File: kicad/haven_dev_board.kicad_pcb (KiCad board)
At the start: 6 copper layers, 72.9 x 160.9 mm, 89 parts, among them CN1 BM46B-12DS-0.35V(51).1, J1 CLE-107-01-G-DV.1, Q1 CSD23382F4.1, Q2 CSD13380F3T.1, Q3 CSD13380F3T.1, SW1 TS2819A 230GF.1, U1 BMX160.1, U10 SN74AXC4T774RSVR.1, U12 GT-USB-9047A.1, U13 SPH0641LU4H-1.1, U14 MX25R6435FBFIL0.1, U15 ADAU1860BCBZRL.1, U2 BQ25120AYFPR.1, U3 AP22916BCA4-7.1, U4 XL-0201SURC.1, U5 KTD2026.1, U6 BQ27220YZFR.1, U8 1MΩ.1, U9 AP22916BCA4-7.1, X1 Q13FC1350000200.1

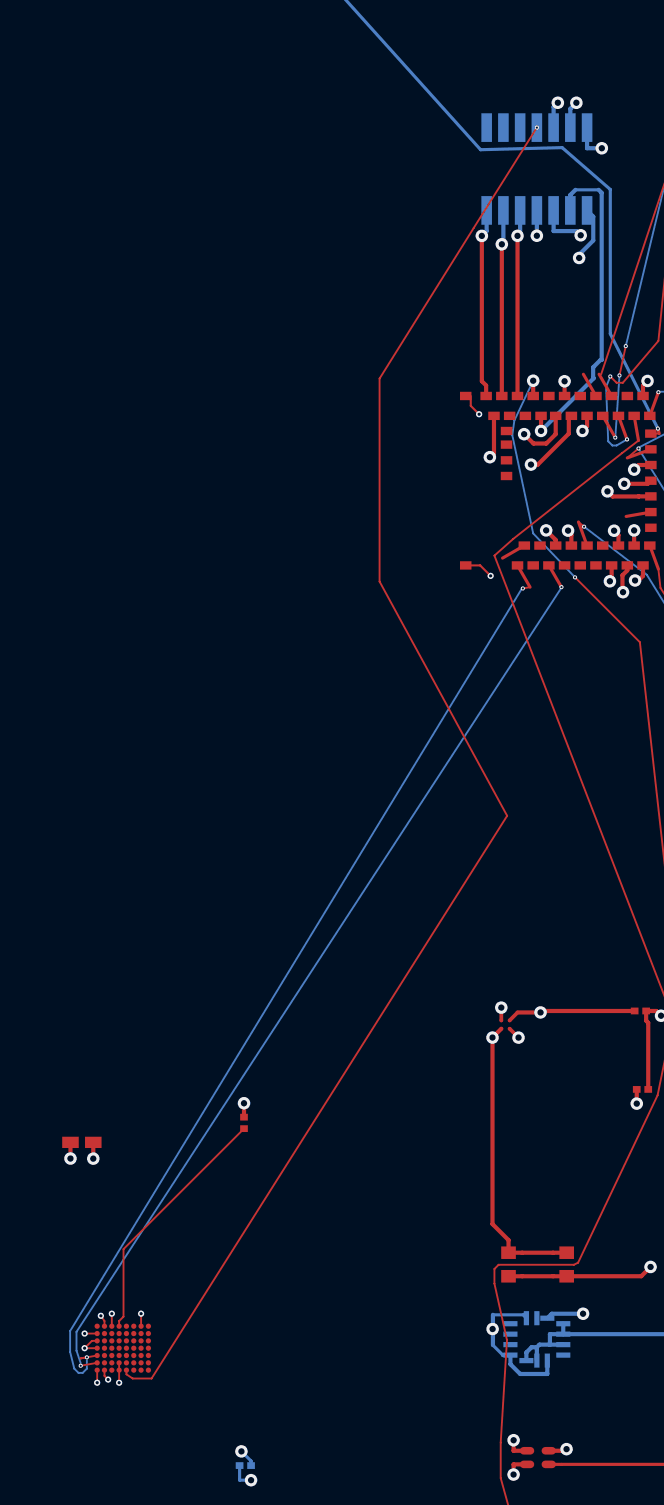
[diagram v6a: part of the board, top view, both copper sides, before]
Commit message: Build a bus-aware router; confirms TDI/TDO/TMS are genuinely blocked
Added tools/bus_router.py: routes a group of related nets together
(hardest-first ordering, each member seen as a real obstacle by
whichever routes after it) instead of one at a time, which is what
TCK/TDI/TDO/TMS actually needed -- net-by-net routing let TCK claim
the one shared escape lane and left the other three with nothing.

Two real bugs caught and fixed while building it, before trusting any
output: the endpoint-layer-fix helper computed a via position but
never added the actual connecting jog track to reach it (would have
silently disconnected the via from the true pad); and the single-layer
fast path was skipped whenever a net's start/end pads were on
different real layers, forcing the much slower general multi-layer
search even in cases (like TCK) where a fast single-layer attempt
already works fine once the wrong-layer landing is corrected
afterward -- exactly the technique used by hand earlier this session.

Extended multilayer_route.py with multilayer_astar_mixed and route_bus
with a mutual_clearance_mm option, so bus siblings can be told to run
tighter to each other than to unrelated copper (standard practice for
a real bus) without a global clearance relaxation.

Ran the actual test: hardest-first ordering alone placed TCK but left
TDI/TDO/TMS with no path at all (100k+ search states exhausted each,
not a resource limit). Adding mutual sibling clearance down to 0.05mm
between all four -- about as tight as anything used elsewhere this
session -- still left all three with nothing. This is a genuine
physical capacity limit, not an ordering or clearance-scoping problem:
the shared corridor is only wide enough for one trace's worth of
copper plus its required margins, confirmed by actual computation
rather than assumed. TDI, TDO, TMS move to the confirmed-blocked list
alongside the other BGA-interior pads -- a placement decision, not a
routing task, would be needed to free real room for 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
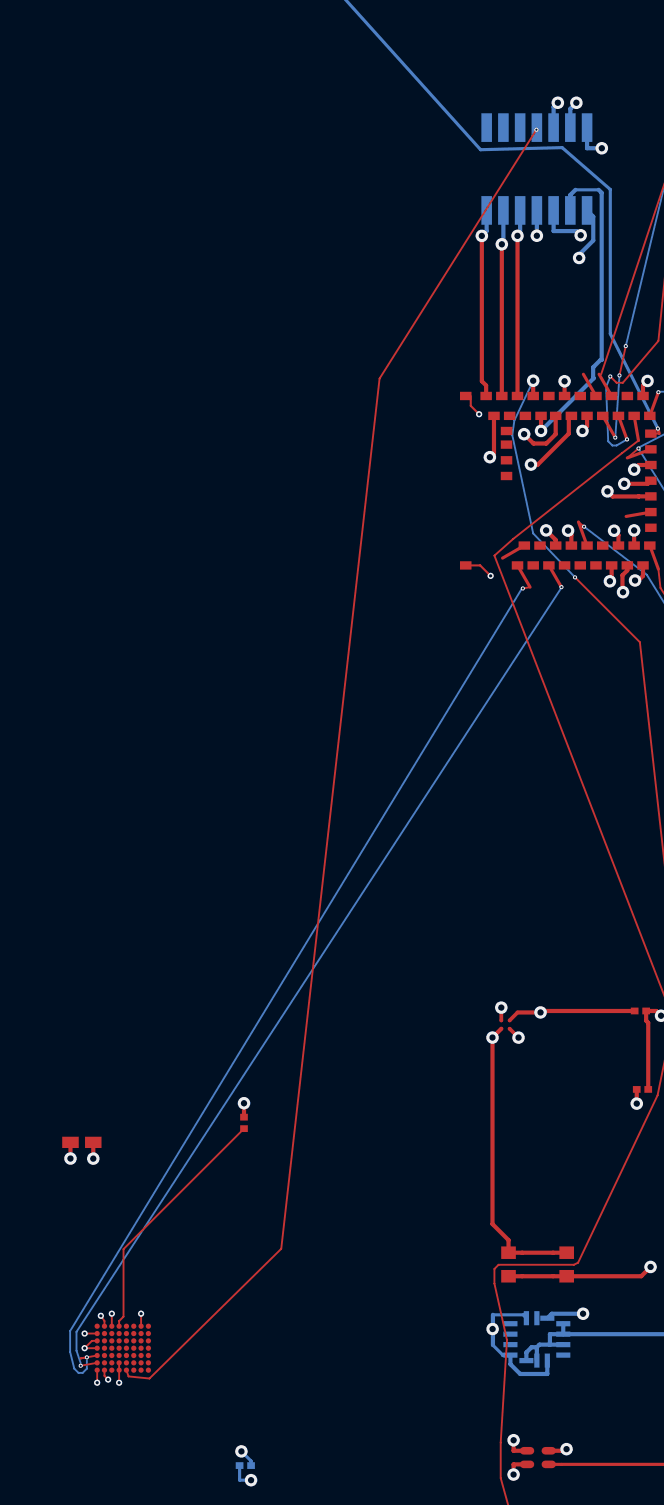
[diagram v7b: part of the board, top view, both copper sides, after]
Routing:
- net TCK: track 69.9 -> 66.2 mm
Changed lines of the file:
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@@
 	)
 	(segment
-		(start 58.7904 112.4979)
-		(end 58.7904 112.6977)
+		(start 58.8904 112.7977)
+		(end 59.8904 112.8977)
 		(width 0.09)
 		(layer "F.Cu")
@@
 	)
 	(segment
-		(start 75.3904 57.8977)
-		(end 78.4102 53.0977)
+		(start 58.7904 112.4979)
+		(end 58.7904 112.4977)
 		(width 0.09)
 		(layer "F.Cu")
@@
 	)
 	(segment
-		(start 58.7904 112.6977)
-		(end 59.090399 112.8977)
+		(start 59.8904 112.8977)
+		(end 66.1904 106.6977)
 		(width 0.09)
 		(layer "F.Cu")
@@
 	(segment
 		(start 70.8904 65.0977)
-		(end 75.3904 57.8977)
+		(end 78.3904 53.1977)
 		(width 0.09)
 		(layer "F.Cu")
@@
 	)
 	(segment
-		(start 59.090399 112.8977)
-		(end 59.9904 112.8977)
-		(width 0.09)
-		(layer "F.Cu")
-		(net 66)
-	)
-	(segment
-		(start 70.8904 74.7977)
+		(start 66.1904 106.6977)
 		(end 70.8904 65.0977)
 		(width 0.09)
@@
 	)
 	(segment
-		(start 59.9904 112.8977)
-		(end 76.9904 85.9977)
-		(width 0.09)
-		(layer "F.Cu")
-		(net 66)
-	)
-	(segment
-		(start 76.9904 85.9977)
-		(end 70.8904 74.7977)
+		(start 58.7904 112.4977)
+		(end 58.8904 112.7977)
 		(width 0.09)
 		(layer "F.Cu")
@@
 	)
 	(via
-		(at 78.4102 53.0977)
+		(at 78.3904 53.1977)
 		(size 0.2)
 		(drill 0.1)
@@
 		(net 66)
 	)
+	(segment
+		(start 78.3904 53.1977)
+		(end 78.4102 53.0977)
+		(width 0.09)
+		(layer "B.Cu")
+		(net 66)
+	)

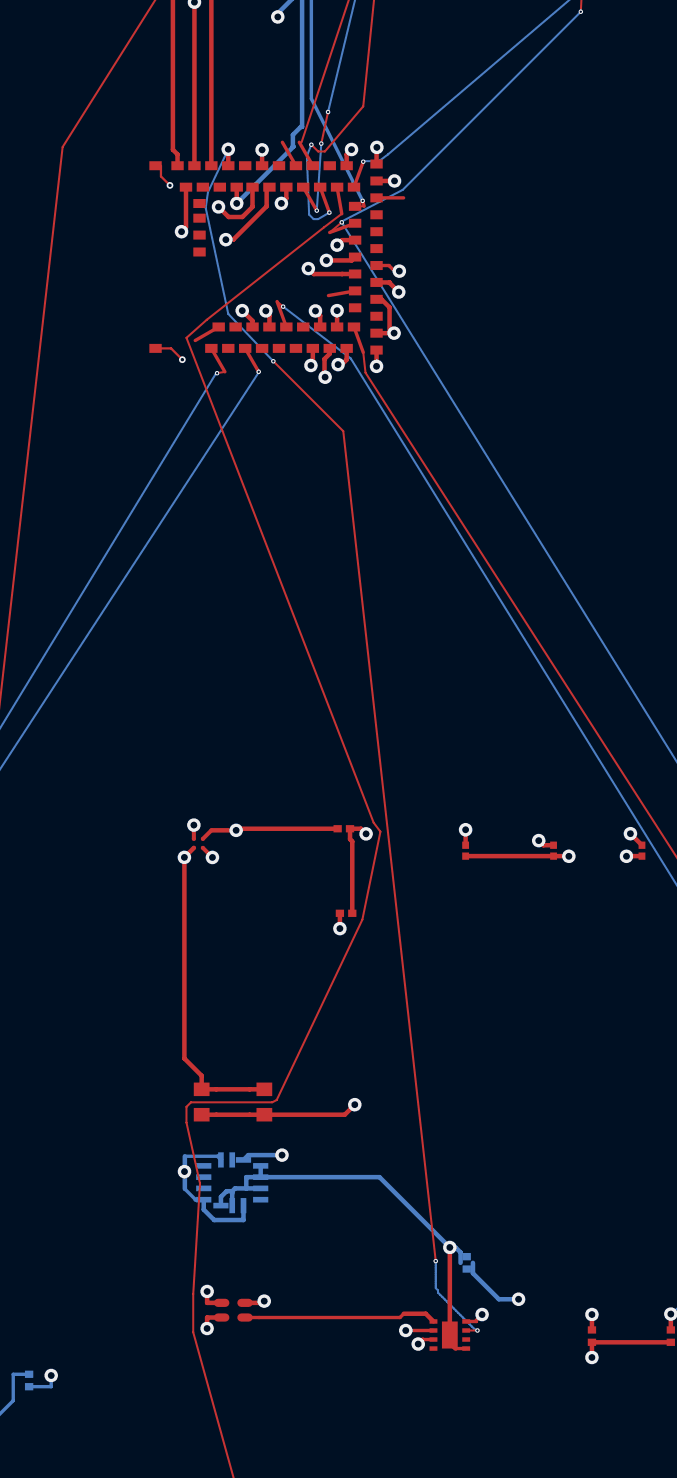
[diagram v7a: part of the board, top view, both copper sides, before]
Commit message: Route SDA (MDBT531-U5): fix a real zone-clearance workflow gap
The MDBT531-to-U5 SDA link was previously reported as walled off (a
flood-fill from the MDBT531 side supposedly reached only a tiny 6x4mm
pocket). Re-running a full-region flood-fill this session found that
claim was stale/wrong -- the whole path between MDBT531 and U5 is
reachable, and multilayer_astar finds a real route.

Placing it first surfaced a genuine, previously-unknown gap: two of the
board's four inner layers are near-full-board GND pours, and via_clear
never checked vias against filled zone copper at all -- only pads and
tracks. Adding a via near U5 triggered 8 new zone-clearance violations
(23 instances) on the first attempt.

Tried making zone fills hard obstacles in route_lib.py's obstacle
collectors, but that produces false negatives: checking a new via
against the *stale* fill (computed before the via existed) makes any
via anywhere near a ground pour look permanently blocked, even though
187 vias already coexist fine with these same pours via the fill
algorithm's automatic per-via clearance carve-out. Reverted that and
added `route_lib.refill_zones()` instead -- call it after placing new
copper and before Save()/DRC, so the saved fill polygons are accurate.
With that, the same route is 0 new violations, 40->39 unconnected.

Co-Authored-By: Claude Sonnet 5 <noreply@anthropic.com>
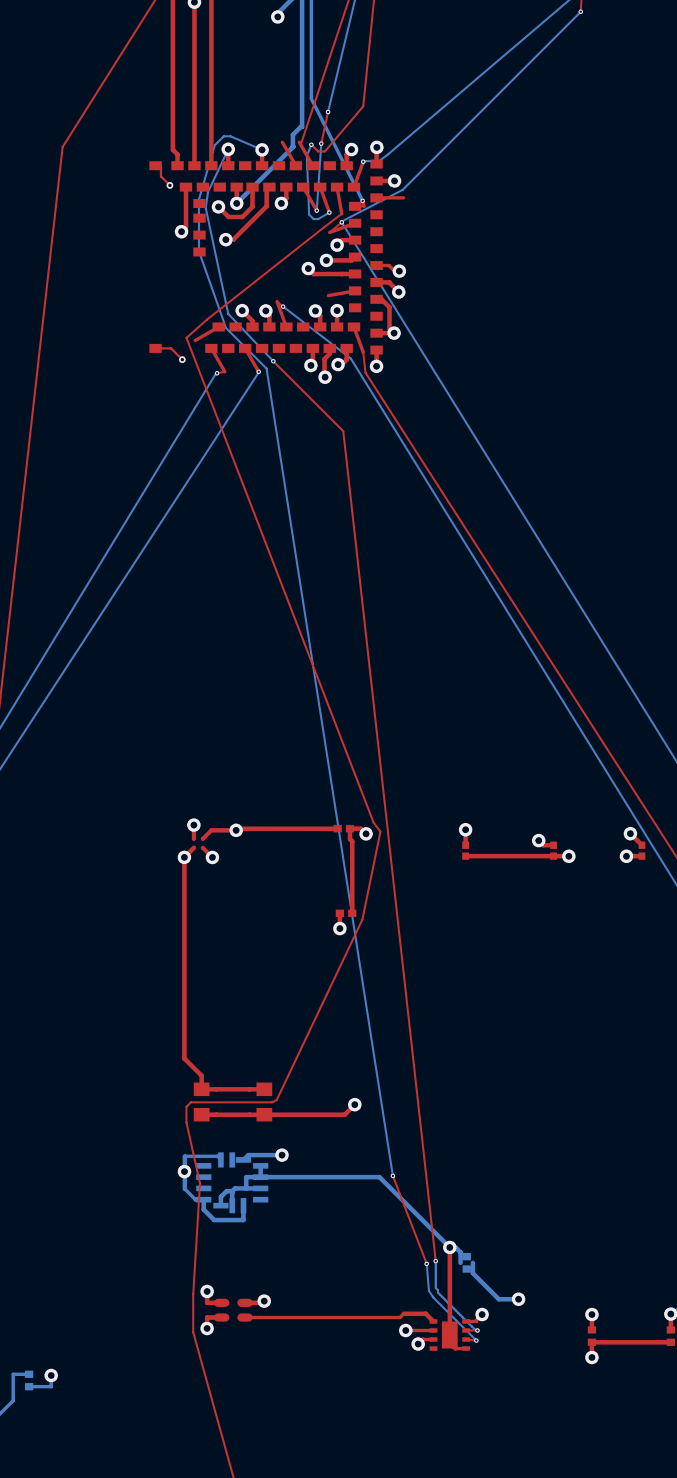
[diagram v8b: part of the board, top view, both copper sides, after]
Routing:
- net SDA: track 69.3 -> 127.7 mm, vias 3 -> 6
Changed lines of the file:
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@@
+	)
+	(segment
+		(start 85.535299 110.7235)
+		(end 87.035299 114.6235)
+		(width 0.09)
+		(layer "F.Cu")
+		(net 47)
+	)
+	(segment
+		(start 89.2353 118.0235)
+		(end 88.7848 117.9777)
+		(width 0.09)
+		(layer "F.Cu")
+		(net 47)
 	)
 	(segment
@@
 	)
 	(via
+		(at 87.035299 114.6235)
+		(size 0.2)
+		(drill 0.1)
+		(layers "F.Cu" "B.Cu")
+		(net 47)
+	)
+	(via
 		(at 51.5789 28.6072)
 		(size 0.6)
@@
 	)
 	(via
+		(at 85.535299 110.7235)
+		(size 0.2)
+		(drill 0.1)
+		(layers "F.Cu" "B.Cu")
+		(net 47)
+	)
+	(via
 		(at 79.7353 65.2235)
 		(size 0.6)
@@
 		(layers "F.Cu" "B.Cu")
 		(locked yes)
+		(net 47)
+	)
+	(via
+		(at 89.2353 118.0235)
+		(size 0.2)
+		(drill 0.1)
+		(layers "F.Cu" "B.Cu")
+		(net 47)
+	)
+	(segment
+		(start 87.035299 114.6235)
+		(end 87.1353 115.8235)
+		(width 0.09)
+		(layer "B.Cu")
+		(net 47)
+	)
+	(segment
+		(start 87.1353 115.8235)
+		(end 87.335299 116.1235)
+		(width 0.09)
+		(layer "B.Cu")
 		(net 47)
 	)
@@
 	)
 	(segment
+		(start 79.7353 65.2235)
+		(end 78.335299 64.6235)
+		(width 0.09)
+		(layer "B.Cu")
+		(net 47)
+	)
+	(segment
+		(start 78.335299 64.6235)
+		(end 78.035299 64.6235)
+		(width 0.09)
+		(layer "B.Cu")
+		(net 47)
+	)
+	(segment
+		(start 78.035299 64.6235)
+		(end 77.6353 65.0235)
+		(width 0.09)
+		(layer "B.Cu")
+		(net 47)
+	)
+	(segment
+		(start 79.9353 74.9235)
+		(end 85.535299 110.7235)
+		(width 0.09)
+		(layer "B.Cu")
+		(net 47)
+	)
+	(segment
+		(start 76.9353 67.4235)
+		(end 76.9353 69.7235)
+		(width 0.09)
+		(layer "B.Cu")
+		(net 47)
+	)
+	(segment
+		(start 76.9353 69.7235)
+		(end 78.1353 73.1235)
+		(width 0.09)
+		(layer "B.Cu")
+		(net 47)
+	)
+	(segment
+		(start 78.1353 73.1235)
+		(end 79.9353 74.9235)
+		(width 0.09)
+		(layer "B.Cu")
+		(net 47)
+	)
+	(segment
 		(start 51.5789 27.9481)
 		(end 51.5789 28.6072)
@@
 		(layer "B.Cu")
 		(net 47)
+	)
+	(segment
+		(start 77.6353 65.0235)
+		(end 76.9353 67.4235)
+		(width 0.09)
+		(layer "B.Cu")
+		(net 47)
+	)
+	(segment
+		(start 87.335299 116.1235)
+		(end 89.2353 118.0235)
+		(width 0.09)
+		(layer "B.Cu")
+		(net 47)
